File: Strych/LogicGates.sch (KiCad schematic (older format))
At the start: 70 parts, among them Q10 2N2222, Q11 2N2222, Q12 2N2222, Q13 2N2222, Q14 2N2222, Q15 2N2222, Q16 2N2222, Q17 2N2222, Q18 2N2222, Q19 2N2222, Q20 2N2222, Q21 2N2222, Q22 2N2222, Q23 2N2222, Q24 2N2222, Q25 2N2222, Q26 2N2222, Q27 2N2222, Q28 2N2222, Q29 2N2222, Q30 2N2222, Q31 2N2222, Q32 2N2222, Q33 2N2222, Q8 2N2222, Q9 2N2222

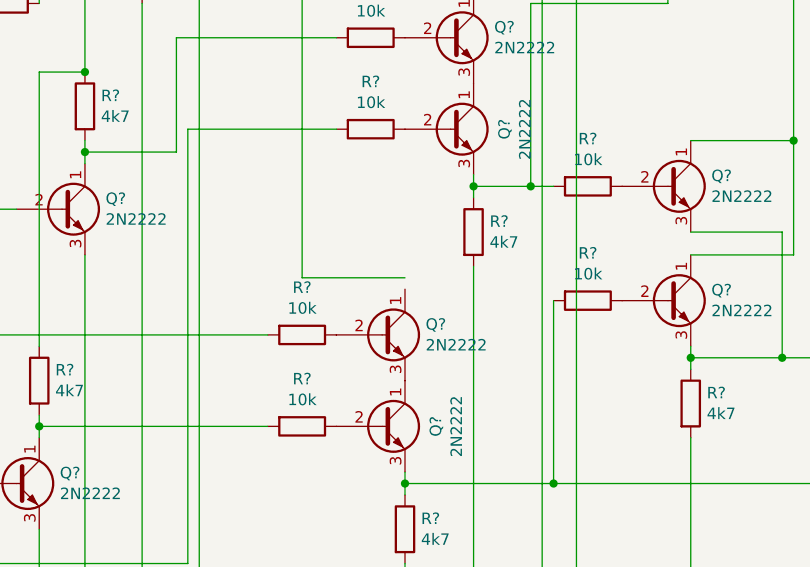
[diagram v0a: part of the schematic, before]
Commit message: Logic gates
Simulated not tested
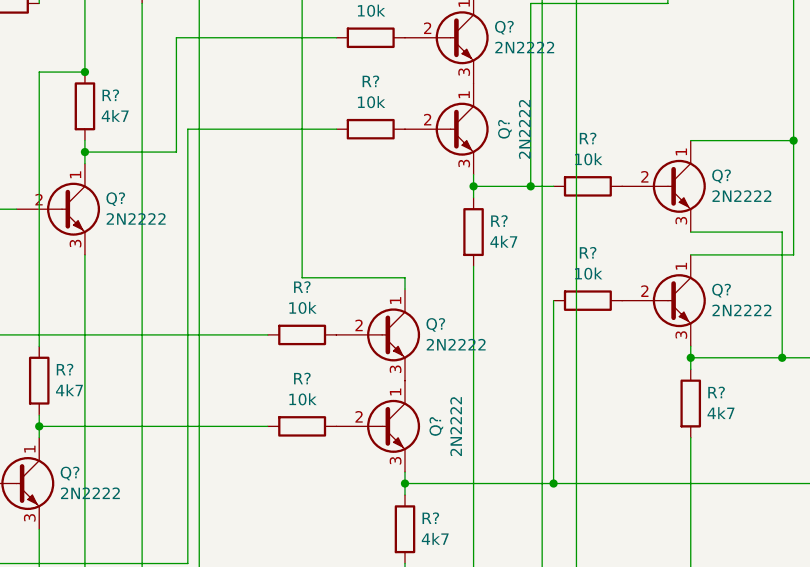
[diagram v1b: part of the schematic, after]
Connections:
- net +5V: now also Q16.1 (C)
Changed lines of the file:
@@
 Text Label 10050 6500 2    50   ~ 0
 GND
+Wire Wire Line
+	6500 4850 6500 4900
 $EndSCHEMATC

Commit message: Strych board v0.1
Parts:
- removed Q29, Q30, Q31, Q32, Q33: 2N2222, Package_TO_SOT_THT:TO-92_Inline, symbol Transistor_BJT:BC237
- added U10, U6, U7, U8, U9: K1010C, Package_DIP:DIP-4_W7.62mm, symbol Isolator:SFH617A-2X009T
- Q10, Q11, Q12, Q13, Q14, Q15, Q16, Q17, Q18, Q19, Q20, Q21, Q22, Q23, Q24, Q25, Q26, Q27, Q28, Q8, Q9: footprint Package_TO_SOT_THT:TO-92_Inline -> Package_TO_SOT_SMD:SOT-23
- R10, R11, R12, R13, R14, R15, R16, R17, R18, R19, R20, R21, R22, R23, R24, R25, R26, R27, R28, R29, R30, R31, R32, R33, R34, R35, R36, R37, R38, R39, R40, R41, R42, R43, R44, R45, R46, R8, R9: footprint (none) -> Resistor_SMD:R_1206_3216Metric
- R47, R48, R49, R50, R51: value 4k7 -> 100; footprint (none) -> Resistor_THT:R_Axial_DIN0204_L3.6mm_D1.6mm_P7.62mm_Horizontal
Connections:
- net GND: now also U10.2, U6.2, U7.2, U8.2, U9.2
- net at R50.1: now also U9.1
- net at R49.1: now also U8.1
- net at R47.1: now also U6.1
- net at R48.1: now also U7.1
- net at R51.1: now also U10.1
